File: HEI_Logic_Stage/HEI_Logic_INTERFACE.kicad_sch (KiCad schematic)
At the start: 51 parts, among them IC2 TLV9004IDR, J10 Conn_02x07_Counter_Clockwise, J4 430450813_Molex, J9 Conn_02x07_Counter_Clockwise, U15 TLV9001IDCKR, U9 CD40109BQNSRQ1

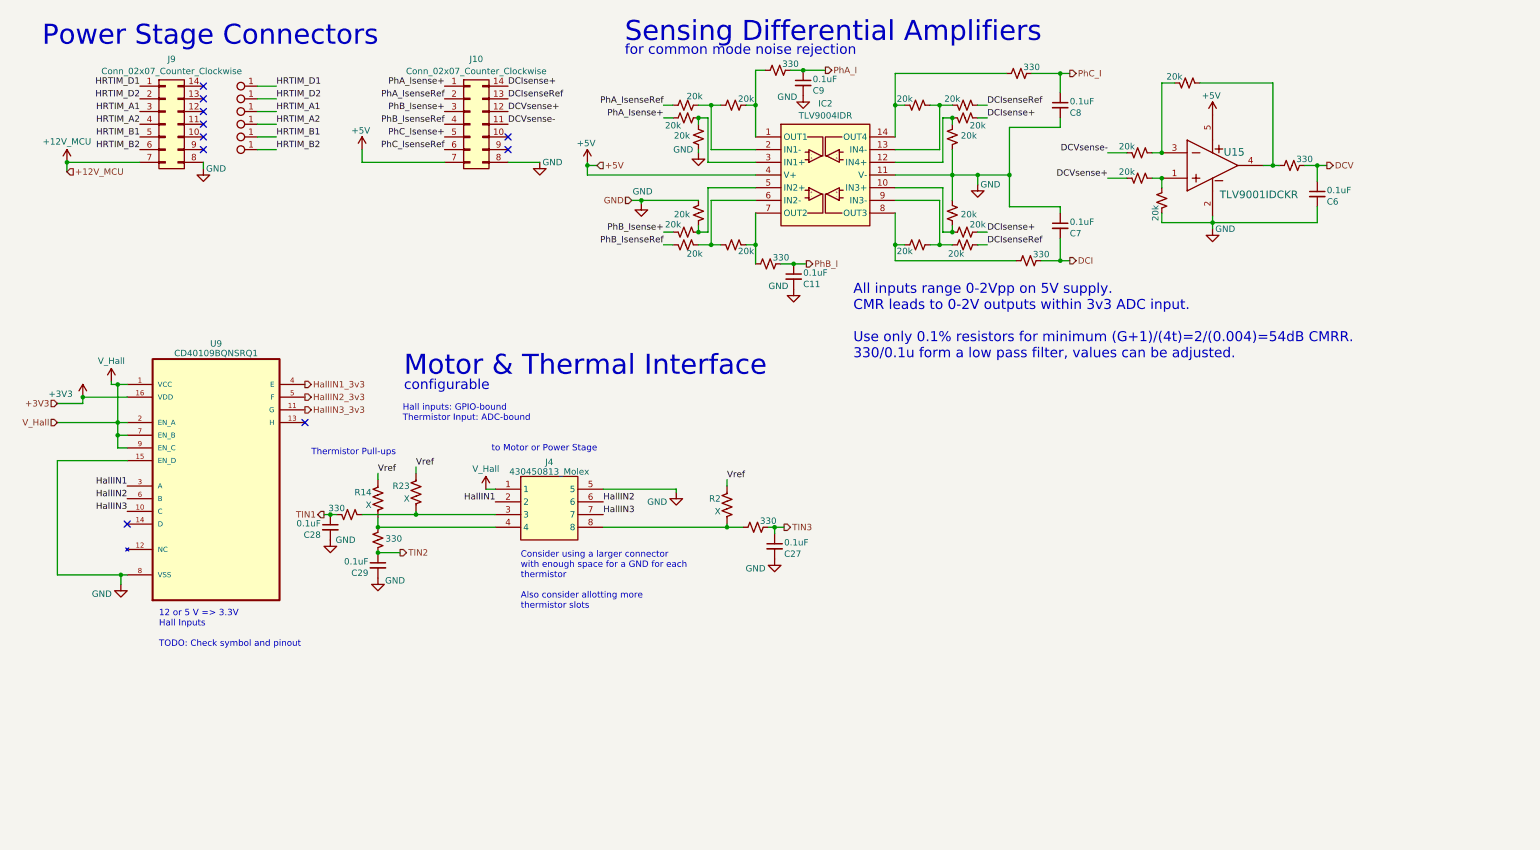
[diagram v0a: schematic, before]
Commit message: new parts into Parts
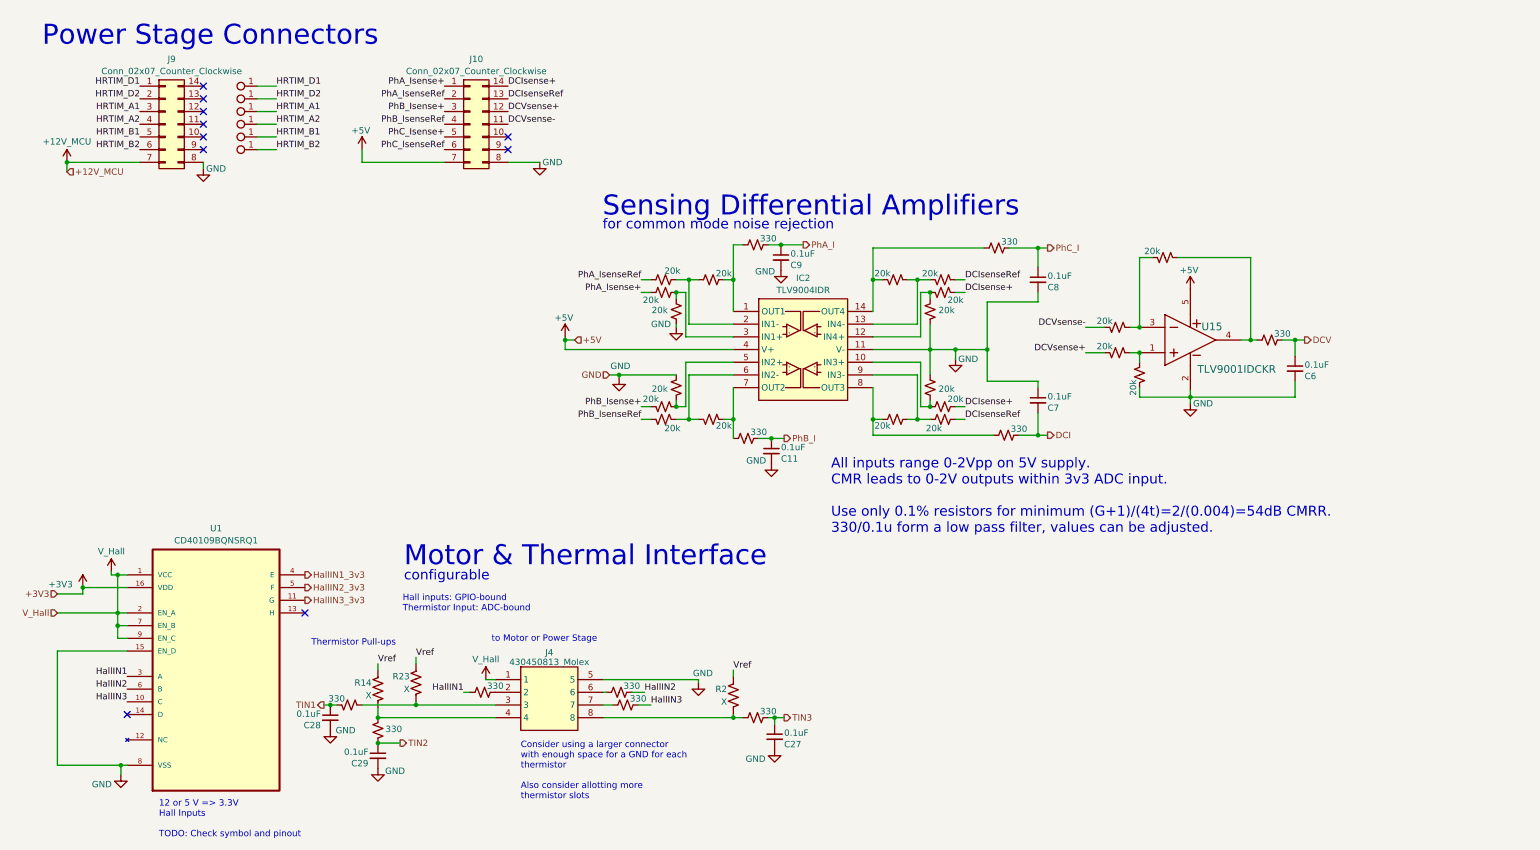
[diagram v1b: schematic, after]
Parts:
- removed U9: CD40109BQNSRQ1, GTSR_KiCAD_Footprints:SOIC127P780X200-16N, symbol CD40109B-Q1:CD40109BQNSRQ1
- added R15, R22, R24: 330, Resistor_SMD:R_0603_1608Metric_Pad0.98x0.95mm_HandSolder, symbol Device:R_Small_US
- added U1: CD40109BQNSRQ1, HEI_Logic:SOIC127P780X200-16N, symbol HEI_Logic:CD40109BQNSRQ1
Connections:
- net +3V3: now also U1.16 (VDD)
- net GND: now also U1.15 (EN_D), U1.8 (VSS)
- net HallIN1: now also R15.1, U1.3 (A); no longer J4.2
- net HallIN1_3v3: now also U1.4 (E)
- net HallIN2: now also R22.2, U1.6 (B); no longer J4.6
- net HallIN2_3v3: now also U1.5 (F)
- net HallIN3: now also R24.2, U1.10 (C); no longer J4.7
- net HallIN3_3v3: now also U1.11 (G)
- net V_Hall: now also U1.1 (VCC), U1.2 (EN_A), U1.7 (EN_B), U1.9 (EN_C)
- new net: J4.2, R15.2
- new net: J4.6, R22.1
- new net: J4.7, R24.1
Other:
- moved on the sheet: C11, C27, C28, C29, C6, C7, C8, C9, IC2, J4, R14, R2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

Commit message: more minor updates
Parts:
- added C1, C2, C3, C4: 0.1uF, Capacitor_SMD:C_0603_1608Metric_Pad1.08x0.95mm_HandSolder, symbol Device:C_Small
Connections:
- net +3V3: now also C3.1
- net +5V: now also C1.1, C2.1
- net GND: now also C1.2, C2.2, C3.2, C4.2
- net V_Hall: now also C4.1
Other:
- note added: "HFI Logic Stage Control/Motor Interface"

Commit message: fixed logic stage diff amp updates + sim
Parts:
- removed C11: 0.1uF, Capacitor_SMD:C_0603_1608Metric_Pad1.08x0.95mm_HandSolder, symbol Device:C_Small
- removed IC2: TLV9004IDR, HEI_Logic:SOIC127P600X175-14N, symbol HEI_Logic:TLV9004IDR
- removed U15: TLV9001IDCKR, HEI_Logic:DCK0005A_M, symbol HEI_Logic:TLV9001IDCKR
- added C30, C31, C32, C34, C35, C36, C37: 0, Capacitor_SMD:C_0603_1608Metric_Pad1.08x0.95mm_HandSolder, symbol Device:C_Small
- added C33, C38, C5: 33p, Capacitor_SMD:C_0603_1608Metric_Pad1.08x0.95mm_HandSolder, symbol Device:C_Small
- added IC1: TLV9054IPWR, HEI_Logic:SOP65P640X120-14N, symbol HEI_Logic:TLV9054IPWR
- added IC2: TLV9051IDBVR, HEI_Logic:SOT95P280X145-5N, symbol HEI_Logic:TLV9051IDBVR
- added R25, R26, R38, R39, R43, R44, R70, R71, R72, R73, R75: 10k, Resistor_SMD:R_0603_1608Metric_Pad0.98x0.95mm_HandSolder, symbol Device:R_Small_US
- added R36, R37, R66, R67: 40k, Resistor_SMD:R_0603_1608Metric_Pad0.98x0.95mm_HandSolder, symbol Device:R_Small_US
- added R40, R68: 25k, Resistor_SMD:R_0603_1608Metric_Pad0.98x0.95mm_HandSolder, symbol Device:R_Small_US
- added R41, R69: 30k, Resistor_SMD:R_0603_1608Metric_Pad0.98x0.95mm_HandSolder, symbol Device:R_Small_US
- added R42, R74, R76, R77: 120, Resistor_SMD:R_0603_1608Metric_Pad0.98x0.95mm_HandSolder, symbol Device:R_Small_US
- C6, C8: value 0.1uF -> 33p
- C7, C9: value 0.1uF -> 0
- R28, R29, R30: value 330 -> 10k
- R31, R32: value 330 -> 40k
- R46, R53: value 20k -> 25k
- R47, R54: value 20k -> 30k
- R48, R49, R50, R56, R57, R58, R59, R60, R61: value 20k -> 10k
- R51, R52, R62, R63, R65: value 20k -> 40k
- R55: value 20k -> 120
- R64: value 20k -> 35k
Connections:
- net +3V3: now also C1.1, C2.1, IC1.4 (V+), IC2.5 (V+)
- net +5V: no longer C1.1, C2.1
- net DCI: now also C38.1, R76.2; no longer C7.2, R29.2
- net DCIsense+: now also R49.2, R52.1; no longer R59.1, R60.1
- net DCIsenseRef: now also R50.2, R51.1; no longer R58.1, R61.1
- net DCV: now also R77.2; no longer R28.2
- net GND: now also R28.1, R29.1, R30.1, R48.1, R49.1, R59.1, R61.1, C31.1, C33.2, C35.1, C36.1, C37.1, C38.2, C5.2, IC1.11 (V-), IC2.2 (V-), R26.1, R38.1, R39.1, R43.1, R44.1, R70.1, R72.1, R73.1, R75.1; no longer C7.1, C9.2, R51.1, R56.1, R64.2
- net PhA_I: now also C5.1, R42.2; no longer C9.1, R31.2
- net PhA_Isense+: now also R37.1, R38.2; no longer R47.1
- net PhA_IsenseRef: now also R36.1, R39.2; no longer R46.1
- net PhB_I: now also C33.1, R74.2; no longer R32.2
- net PhB_Isense+: now also R43.2, R67.1; no longer R48.1
- net PhB_IsenseRef: now also R44.2, R66.1; no longer R49.1
- net PhC_I: now also R55.2; no longer R30.2
- net PhC_Isense+: now also R29.2, R32.1
- net PhC_IsenseRef: now also R30.2, R31.1
- net Vref: now also R56.2, R58.2, R60.2, R25.2, R71.2
- net C+: now reaches R46.2
- net C+: now also R32.2, C37.2, IC1.10 (IN3+); no longer R52.1
- net D+: now reaches R52.2
- net D+: now also C35.2, IC1.12 (IN4+), R68.2; no longer R31.1
- net D-: now reaches R54.1
- net D-: now also C9.1, R51.2, IC1.13 (IN4-); no longer R58.2
- net Do: now reaches R54.2
- net Do: now also C9.2, IC1.14 (OUT4), R75.2, R76.1; no longer R30.1
- net Co: now reaches R47.2
- net Co: now also C7.2, R48.2, R55.1, IC1.8 (OUT3); no longer R50.2
- net E+: now reaches R63.1, R64.1
- net E+: now also IC2.3 (IN+)
- net at R59.2: now also R58.1, R68.1; no longer R56.2
- net at R57.2: now also R56.1, R40.1; no longer R60.2
- net E-: now reaches R62.1, R65.2
- net E-: now also C34.1, IC2.4 (IN-)
- net Eo: now reaches R65.1
- net Eo: now also R28.2, C34.2, IC2.1 (OUT), R77.1; no longer R28.1
- net at R61.2: now also R46.1, R60.1; no longer R55.1
- net B+: now reaches R53.2
- net B+: now also C36.2, IC1.5 (IN2+), R67.2; no longer R32.1
- net at R53.1: now also R25.1, R26.2; no longer R49.2
- new net: R64.2, R71.1, R72.2
- new net A+: C31.2, IC1.3 (IN1+), R37.2, R40.2
- new net A-: C30.1, IC1.2 (IN1-), R36.2, R41.1
- new net Ao: C30.2, IC1.1 (OUT1), R41.2, R42.1, R73.2
- new net B-: C32.1, IC1.6 (IN2-), R66.2, R69.1
- new net Bo: C32.2, IC1.7 (OUT2), R69.2, R70.2, R74.1
- new net C-: C7.1, IC1.9 (IN3-), R31.2, R47.1
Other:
- note added: "0.75 gain differential stage with 1.65V Vocm offset (3v3 single supply) (high impedance resistances) (use 0.1% resistors)"
- note added: "Current inputs: 0.55V-4.45V, centered at 2.55V (ZCR) - diff amp with gain of 3/4 transforms to ~3Vpp centered on Vocm Vocm = 1.65V (half of 3v3) DCVsense input ranges 0-2Vpp with 1.44 Vcm. Diff amplifier with unity gain transforms to 0-2Vpp centered on Vocm. Vocm generated through resistor divider and feedback network around op amps. 10k divider also acts as part of lower resistor for non-inv inp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"
- note added: "Hall outputs able to source and sink current (3mA sink to 5.5mA source, sense out) (14mA sink to 2mA source, ref out) Input 10k resistors satisfy minimum resistive load of Halls."
- note added: "Op amp selection verified using LTspice 15 V/us slew rate, 5 MHz unity gain bandwidth, RRIO, up to 5.5V supply"
- note added: "Optional filter + min. resistive load for op amp"
- note added: "▷"
- note removed: "All inputs range 0-2Vpp on 5V supply. CMR leads to 0-2V outputs within 3v3 ADC input. Use only 0.1% resistors for minimum (G+1)/(4t)=2/(0.004)=54dB CMRR. 330/0.1u form a low pass filter, values can be adjusted."
- moved on the sheet: C1, C2, C27, C28, C29, C3, C4, J4, R14, R2, R23, U1

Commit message: vertical logic stage complete
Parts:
- removed IC1: TLV9054IPWR, HEI_Logic:SOP65P640X120-14N, symbol HEI_Logic:TLV9054IPWR
- removed J10, J9: Conn_02x07_Counter_Clockwise, symbol Connector_Generic:Conn_02x07_Counter_Clockwise
- added C11, C39, C40: 0.1uF, Capacitor_SMD:C_0603_1608Metric_Pad1.08x0.95mm_HandSolder, symbol Device:C_Small
- added C41: 33p, Capacitor_SMD:C_0402_1005Metric_Pad0.74x0.62mm_HandSolder, symbol Device:C_Small
- added J1, J2: Conn_02x07_Odd_Even, Connector_PinHeader_2.54mm:PinHeader_2x07_P2.54mm_Horizontal, symbol Connector_Generic:Conn_02x07_Odd_Even
- added R78: 10k, Resistor_SMD:R_0402_1005Metric_Pad0.72x0.64mm_HandSolder, symbol Device:R_Small_US
- added R79: 120, Resistor_SMD:R_0402_1005Metric_Pad0.72x0.64mm_HandSolder, symbol Device:R_Small_US
- added U3, U4, U7, U8: TLV9051IDBVR, HEI_Logic:SOT95P280X145-5N, symbol HEI_Logic:TLV9051IDBVR
- C30, C31, C32, C33, C34, C35, C36, C37, C38, C5, C7: footprint Capacitor_SMD:C_0603_1608Metric_Pad1.08x0.95mm_HandSolder -> Capacitor_SMD:C_0402_1005Metric_Pad0.74x0.62mm_HandSolder
- C6, C8: value 33p -> 0; footprint Capacitor_SMD:C_0603_1608Metric_Pad1.08x0.95mm_HandSolder -> Capacitor_SMD:C_0402_1005Metric_Pad0.74x0.62mm_HandSolder
- C9: value 0 -> 33p; footprint Capacitor_SMD:C_0603_1608Metric_Pad1.08x0.95mm_HandSolder -> Capacitor_SMD:C_0402_1005Metric_Pad0.74x0.62mm_HandSolder
- R25, R26, R28, R29, R30, R31, R32, R36, R37, R38, R39, R40, R41, R42, R43, R44, R49, R50, R53, R56, R57, R59, R63, R66, R67, R69, R70, R73, R74, R75, R76: footprint Resistor_SMD:R_0603_1608Metric_Pad0.98x0.95mm_HandSolder -> Resistor_SMD:R_0402_1005Metric_Pad0.72x0.64mm_HandSolder
- R46, R68: value 25k -> 10k; footprint Resistor_SMD:R_0603_1608Metric_Pad0.98x0.95mm_HandSolder -> Resistor_SMD:R_0402_1005Metric_Pad0.72x0.64mm_HandSolder
- R47: value 30k -> 25k; footprint Resistor_SMD:R_0603_1608Metric_Pad0.98x0.95mm_HandSolder -> Resistor_SMD:R_0402_1005Metric_Pad0.72x0.64mm_HandSolder
- R48, R61, R72: value 10k -> 30k; footprint Resistor_SMD:R_0603_1608Metric_Pad0.98x0.95mm_HandSolder -> Resistor_SMD:R_0402_1005Metric_Pad0.72x0.64mm_HandSolder
- R51: value 40k -> 120; footprint Resistor_SMD:R_0603_1608Metric_Pad0.98x0.95mm_HandSolder -> Resistor_SMD:R_0402_1005Metric_Pad0.72x0.64mm_HandSolder
- R52, R62, R65: value 40k -> 10k; footprint Resistor_SMD:R_0603_1608Metric_Pad0.98x0.95mm_HandSolder -> Resistor_SMD:R_0402_1005Metric_Pad0.72x0.64mm_HandSolder
- R54: value 30k -> 10k; footprint Resistor_SMD:R_0603_1608Metric_Pad0.98x0.95mm_HandSolder -> Resistor_SMD:R_0402_1005Metric_Pad0.72x0.64mm_HandSolder
- R55: value 120 -> 40k; footprint Resistor_SMD:R_0603_1608Metric_Pad0.98x0.95mm_HandSolder -> Resistor_SMD:R_0402_1005Metric_Pad0.72x0.64mm_HandSolder
- R58: value 10k -> 40k; footprint Resistor_SMD:R_0603_1608Metric_Pad0.98x0.95mm_HandSolder -> Resistor_SMD:R_0402_1005Metric_Pad0.72x0.64mm_HandSolder
- R60, R71: value 10k -> 25k; footprint Resistor_SMD:R_0603_1608Metric_Pad0.98x0.95mm_HandSolder -> Resistor_SMD:R_0402_1005Metric_Pad0.72x0.64mm_HandSolder
- R64: value 35k -> 40k; footprint Resistor_SMD:R_0603_1608Metric_Pad0.98x0.95mm_HandSolder -> Resistor_SMD:R_0402_1005Metric_Pad0.72x0.64mm_HandSolder
- R77: value 120 -> 10k; footprint Resistor_SMD:R_0603_1608Metric_Pad0.98x0.95mm_HandSolder -> Resistor_SMD:R_0402_1005Metric_Pad0.72x0.64mm_HandSolder
- renumbered IC2 to U16
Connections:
- net +12V_MCU: now also J1.2 (Pin_2)
- net +3V3: now also C11.1, C39.1, C40.1, U3.5 (V+), U4.5 (V+), U7.5 (V+), U8.5 (V+)
- net +5V: now also J2.2 (Pin_2)
- net A+: now also U3.3 (IN+)
- net A-: now also U3.4 (IN-)
- net Ao: now also U3.1 (OUT)
- net B+: now also U4.3 (IN+)
- net B-: now also U4.4 (IN-)
- net Bo: now also U4.1 (OUT)
- net C+: now also C8.2, R47.2, U7.3 (IN+); no longer C37.2, R46.2
- net C-: now also R48.1, U7.4 (IN-); no longer R47.1
- net Co: now also R50.2, R51.1, U7.1 (OUT); no longer R47.2, R55.1
- net D+: now also C37.2, R58.2, R60.2, U8.3 (IN+); no longer C35.2, R52.2, R68.2
- net D-: now also C35.1, R55.2, R61.1, U8.4 (IN-); no longer C9.1, R51.2, R54.1
- net DCIsense+: now also R52.2, R58.1, J2.8 (Pin_8); no longer R49.2, R52.1
- net DCIsenseRef: now also R54.2, R55.1, J2.10 (Pin_10); no longer R50.2, R51.1
- net DCV: now also C41.1, R79.2; no longer C6.1, R77.2
- net DCVsense+: now also R28.2, R64.1, J2.12 (Pin_12); no longer R63.2
- net DCVsense-: now also R63.1, J2.14 (Pin_14)
- net Do: now also C35.2, R61.2, U8.1 (OUT); no longer C9.2, R54.2
- net E+: now also C34.2, R64.2, R71.2; no longer R63.1, R64.1
- net E-: now also C6.1, R63.2, R72.1; no longer C34.1, R62.1, R65.2
- net Eo: now also C6.2, R72.2, R78.2, R79.1; no longer C34.2, R28.2, R65.1, R77.1
- net GND: now also C34.1, C8.1, C9.2, R52.1, R54.1, R62.1, R68.1, R77.1, C11.2, C39.2, C40.2, C41.2, J1.1 (Pin_1), J2.1 (Pin_1), R78.1, U3.2 (V-), U4.2 (V-), U7.2 (V-), U8.2 (V-); no longer C35.1, C6.2, C8.2, R48.1, R59.1, R61.1, R72.1
- net PhA_Isense+: now also J2.13 (Pin_13)
- net PhA_IsenseRef: now also J2.11 (Pin_11)
- net PhB_Isense+: now also J2.9 (Pin_9)
- net PhB_IsenseRef: now also J2.7 (Pin_7)
- net PhC_I: now also C9.1, R51.2; no longer C8.1, R55.2
- net PhC_Isense+: now also J2.5 (Pin_5)
- net PhC_IsenseRef: now also J2.3 (Pin_3)
- net Vref: now also R46.2, R59.2, R65.2; no longer R58.2, R60.2, R71.2
- net HRTIM_A1 renamed HS_B
- net HS_B: now also J1.9 (Pin_9)
- net HRTIM_A2 renamed LS_B
- net LS_B: now also J1.7 (Pin_7)
- net HRTIM_B1 renamed HS_C
- net HS_C: now also J1.5 (Pin_5)
- net HRTIM_B2 renamed LS_C
- net LS_C: now also J1.3 (Pin_3)
- net HRTIM_D1 renamed HS_A
- net HS_A: now also J1.13 (Pin_13)
- net HRTIM_D2 renamed LS_A
- net LS_A: now also J1.11 (Pin_11)
- new net: R65.1, R71.1, R77.2
- new net: R59.1, R60.1, R68.2
- new net: R46.1, R47.1, R49.2
- no-connect marks 10 -> 4
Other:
- note added: "0.75 gain differential stage with 1.65V Vodc offset (3v3 single supply) (high impedance resistances) (use 0.1% resistors)"
- note added: "Current inputs: 0.55V-4.45V, centered at 2.55V (ZCR) - diff amp with gain of 3/4 transforms to ~3Vpp centered on Vodc Vodc = 1.65V (half of 3v3) DCVsense input ranges 0-2Vpp with 1.44 Vcm. Diff amplifier with unity gain transforms to 0-2Vpp centered on Vodc. Vocm generated through resistor divider and feedback network around op amps. 10k divider also acts as part of lower resistor for non-inv inp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"
- note removed: "0.75 gain differential stage with 1.65V Vocm offset (3v3 single supply) (high impedance resistances) (use 0.1% resistors)"
- note removed: "Current inputs: 0.55V-4.45V, centered at 2.55V (ZCR) - diff amp with gain of 3/4 transforms to ~3Vpp centered on Vocm Vocm = 1.65V (half of 3v3) DCVsense input ranges 0-2Vpp with 1.44 Vcm. Diff amplifier with unity gain transforms to 0-2Vpp centered on Vocm. Vocm generated through resistor divider and feedback network around op amps. 10k divider also acts as part of lower resistor for non-inv inp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"
- moved on the sheet: C1
